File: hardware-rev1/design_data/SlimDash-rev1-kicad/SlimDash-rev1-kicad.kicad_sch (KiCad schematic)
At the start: 70 parts

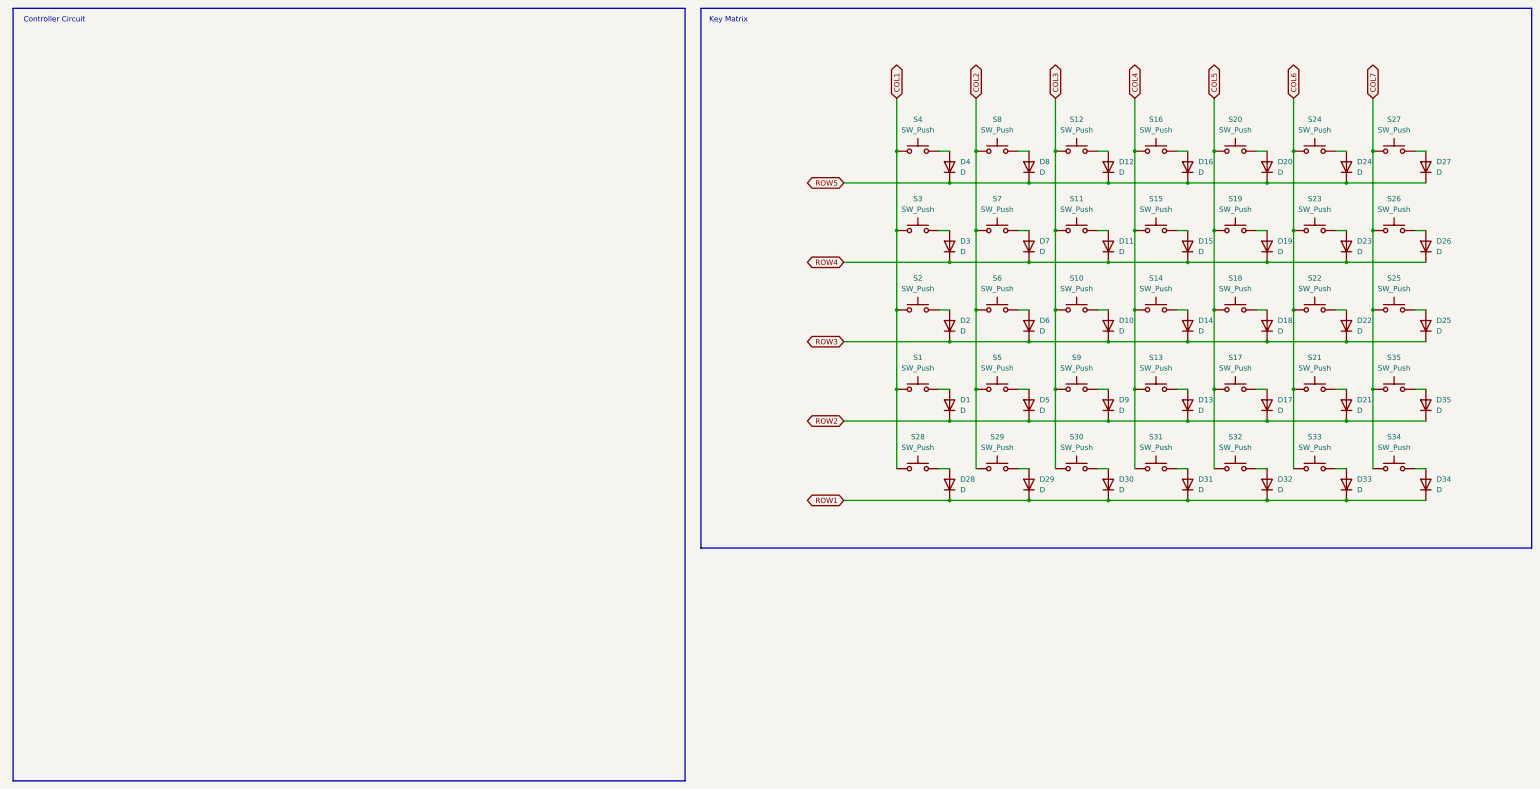
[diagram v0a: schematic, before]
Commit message: fix some positioning and net labels
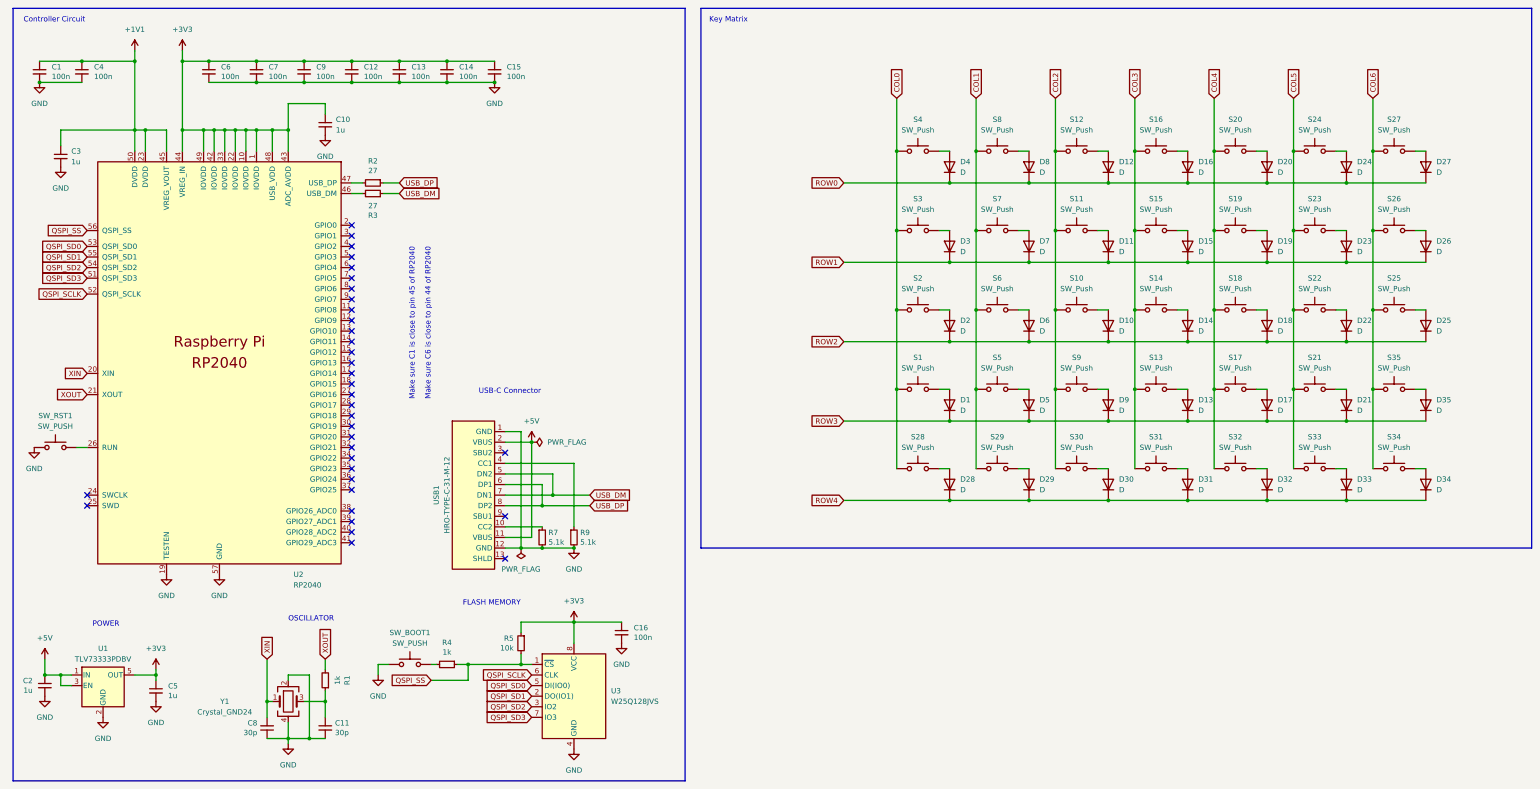
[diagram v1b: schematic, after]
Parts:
- added C1, C12, C13, C14, C15, C16, C4, C6, C7, C9: 100n, Capacitor_SMD:C_0402_1005Metric, symbol Device:C_Small
- added C10, C2, C3, C5: 1u, Capacitor_SMD:C_0402_1005Metric, symbol Device:C_Small
- added C11, C8: 30p, Capacitor_SMD:C_0402_1005Metric, symbol Device:C_Small
- added R1, R4: 1k, Resistor_SMD:R_0402_1005Metric, symbol Device:R_Small
- added R2, R3: 27, Resistor_SMD:R_0402_1005Metric, symbol Device:R_Small
- added R5: 10k, Resistor_SMD:R_0402_1005Metric, symbol Device:R_Small
- added R7, R9: 5.1k, Resistor_SMD:R_0402_1005Metric, symbol Device:R_Small
- added SW_BOOT1, SW_RST1: SW_PUSH, mzm_misc:SW_Tactile_Yushakobo 3x6x4.3mm, symbol Switch:SW_Push
- added U1: TLV73333PDBV, Package_TO_SOT_SMD:SOT-23-5, symbol Regulator_Linear:TLV73333PDBV
- added U2: RP2040, RP2040:RP2040-QFN-56, symbol ergoSHIFT-rev2:RP2040
- added U3: W25Q128JVS, Package_SO:SOIC-8_5.23x5.23mm_P1.27mm, symbol Memory_Flash:W25Q128JVS
- added USB1: HRO-TYPE-C-31-M-12, ai03-2725_Type-C:HRO-TYPE-C-31-M-12-Assembly, symbol ergoSHIFT-rev2:HRO-TYPE-C-31-M-12
- added Y1: Crystal_GND24, Crystal:Crystal_SMD_3225-4Pin_3.2x2.5mm, symbol Device:Crystal_GND24
- D1, D10, D11, D12, D13, D14, D15, D16, D17, D18, D19, D2, D20, D21, D22, D23, D24, D25, D26, D27, D28, D29, D3, D30, D31, D32, D33, D34, D35, D4, D5, D6, D7, D8, D9: footprint (none) -> Diode_SMD:D_SOD-123F; LCSC (none) -> C33962554
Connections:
- net COL7 is gone; now on net COL6: S25.1, S26.1, S27.1, S34.1, S35.1
- net COL1: now also S29.1, S5.1, S6.1, S7.1, S8.1; no longer S1.1, S2.1, S28.1, S3.1, S4.1
- net COL2: now also S10.1, S11.1, S12.1, S30.1, S9.1; no longer S29.1, S5.1, S6.1, S7.1, S8.1
- net COL3: now also S13.1, S14.1, S15.1, S16.1, S31.1; no longer S10.1, S11.1, S12.1, S30.1, S9.1
- net COL4: now also S17.1, S18.1, S19.1, S20.1, S32.1; no longer S13.1, S14.1, S15.1, S16.1, S31.1
- net COL5: now also S21.1, S22.1, S23.1, S24.1, S33.1; no longer S17.1, S18.1, S19.1, S20.1, S32.1
- net COL6: no longer S21.1, S22.1, S23.1, S24.1, S33.1
- net ROW1: now also D11.1 (K), D15.1 (K), D19.1 (K), D23.1 (K), D26.1 (K), D3.1 (K), D7.1 (K); no longer D28.1 (K), D29.1 (K), D30.1 (K), D31.1 (K), D32.1 (K), D33.1 (K), D34.1 (K)
- net ROW2: now also D10.1 (K), D14.1 (K), D18.1 (K), D2.1 (K), D22.1 (K), D25.1 (K), D6.1 (K); no longer D1.1 (K), D13.1 (K), D17.1 (K), D21.1 (K), D35.1 (K), D5.1 (K), D9.1 (K)
- net ROW3: now also D1.1 (K), D13.1 (K), D17.1 (K), D21.1 (K), D35.1 (K), D5.1 (K), D9.1 (K); no longer D10.1 (K), D14.1 (K), D18.1 (K), D2.1 (K), D22.1 (K), D25.1 (K), D6.1 (K)
- net ROW4: now also D28.1 (K), D29.1 (K), D30.1 (K), D31.1 (K), D32.1 (K), D33.1 (K), D34.1 (K); no longer D11.1 (K), D15.1 (K), D19.1 (K), D23.1 (K), D26.1 (K), D3.1 (K), D7.1 (K)
- net ROW5 renamed ROW0
- new net: C11.1, R1.1, Y1.3
- new net: R4.2, SW_BOOT1.2
- new net: R7.1, USB1.10 (CC2)
- new net: R9.1, USB1.4 (CC1)
- new net: SW_RST1.2, U2.26 (RUN)
- new net: R3.2, U2.46 (USB_DM)
- new net: R2.2, U2.47 (USB_DP)
- new net +1V1: C1.1, C3.1, C4.1, U2.23 (DVDD), U2.45 (VREG_VOUT), U2.50 (DVDD)
- new net +3V3: C10.1, C12.1, C13.1, C14.1, C15.1, C16.1, C5.1, C6.1, C7.1, C9.1, R5.1, U1.5 (OUT), U2.1 (IOVDD), U2.10 (IOVDD), U2.22 (IOVDD), U2.33 (IOVDD), U2.42 (IOVDD), U2.43 (ADC_AVDD), U2.44 (VREG_IN), U2.48 (USB_VDD), U2.49 (IOVDD), U3.8 (VCC)
- new net +5V: C2.1, U1.1 (IN), U1.3 (EN), USB1.11 (VBUS), USB1.2 (VBUS)
- new net COL0: S1.1, S2.1, S28.1, S3.1, S4.1
- new net GND: C1.2, C10.2, C11.2, C12.2, C13.2, C14.2, C15.2, C16.2, C2.2, C3.2, C4.2, C5.2, C6.2, C7.2, C8.1, C9.2, R7.2, R9.2, SW_BOOT1.1, SW_RST1.1, U1.2 (GND), U2.19 (TESTEN), U2.57 (GND), U3.4 (GND), USB1.1 (GND), USB1.12 (GND), Y1.2, Y1.4
- new net QSPI_SCLK: U2.52 (QSPI_SCLK), U3.6 (CLK)
- new net QSPI_SD0: U2.53 (QSPI_SD0), U3.5 (DI(IO0))
- new net QSPI_SD1: U2.55 (QSPI_SD1), U3.2 (DO(IO1))
- new net QSPI_SD2: U2.54 (QSPI_SD2), U3.3 (IO2)
- new net QSPI_SD3: U2.51 (QSPI_SD3), U3.7 (IO3)
- new net QSPI_SS: R4.1, R5.2, U2.56 (QSPI_SS), U3.1 (~{CS})
- new net USB_DM: R3.1, USB1.5 (DN2), USB1.7 (DN1)
- new net USB_DP: R2.1, USB1.6 (DP1), USB1.8 (DP2)
- new net XIN: C8.2, U2.20 (XIN), Y1.1
- new net XOUT: R1.2, U2.21 (XOUT)
- no-connect marks 0 -> 35
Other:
- note added: "FLASH MEMORY"
- note added: "Make sure C1 is close to pin 45 of RP2040"
- note added: "Make sure C6 is close to pin 44 of RP2040"
- note added: "OSCILLATOR"
- note added: "POWER"
- note added: "USB-C Connector"

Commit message: add more components to design data
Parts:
- added J1, J2: AudioJack4, Keebio-Parts:TRRS-PJ-320A, symbol Connector_Audio:AudioJack4
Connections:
- net +3V3: now also J1.1, J2.1
- net GND: now also J1.4, J2.4
- new net PIO_RX: J1.2, J2.3
- new net PIO_TX: J1.3, J2.2

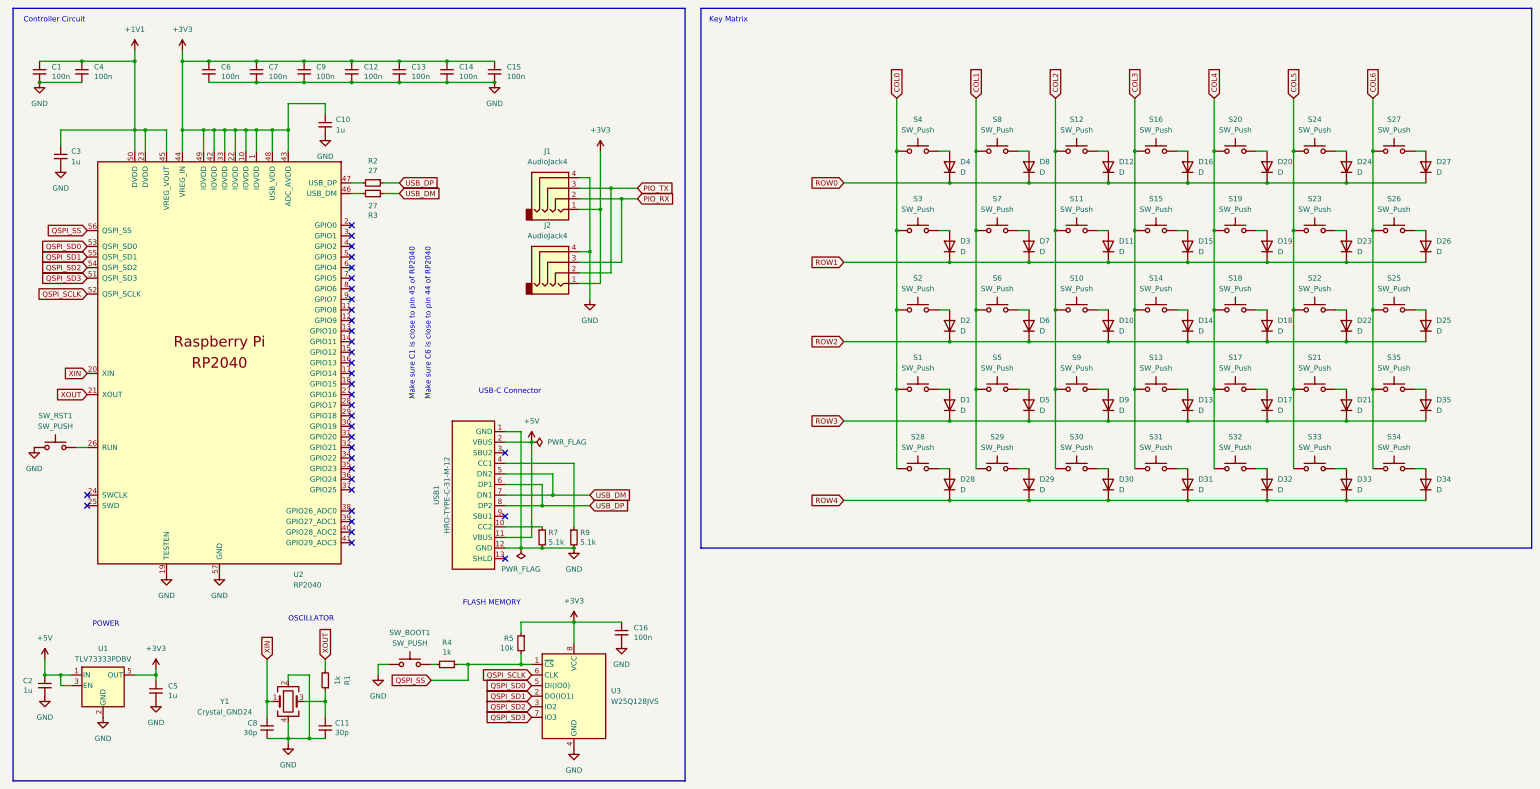
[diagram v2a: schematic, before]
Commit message: add surge protection
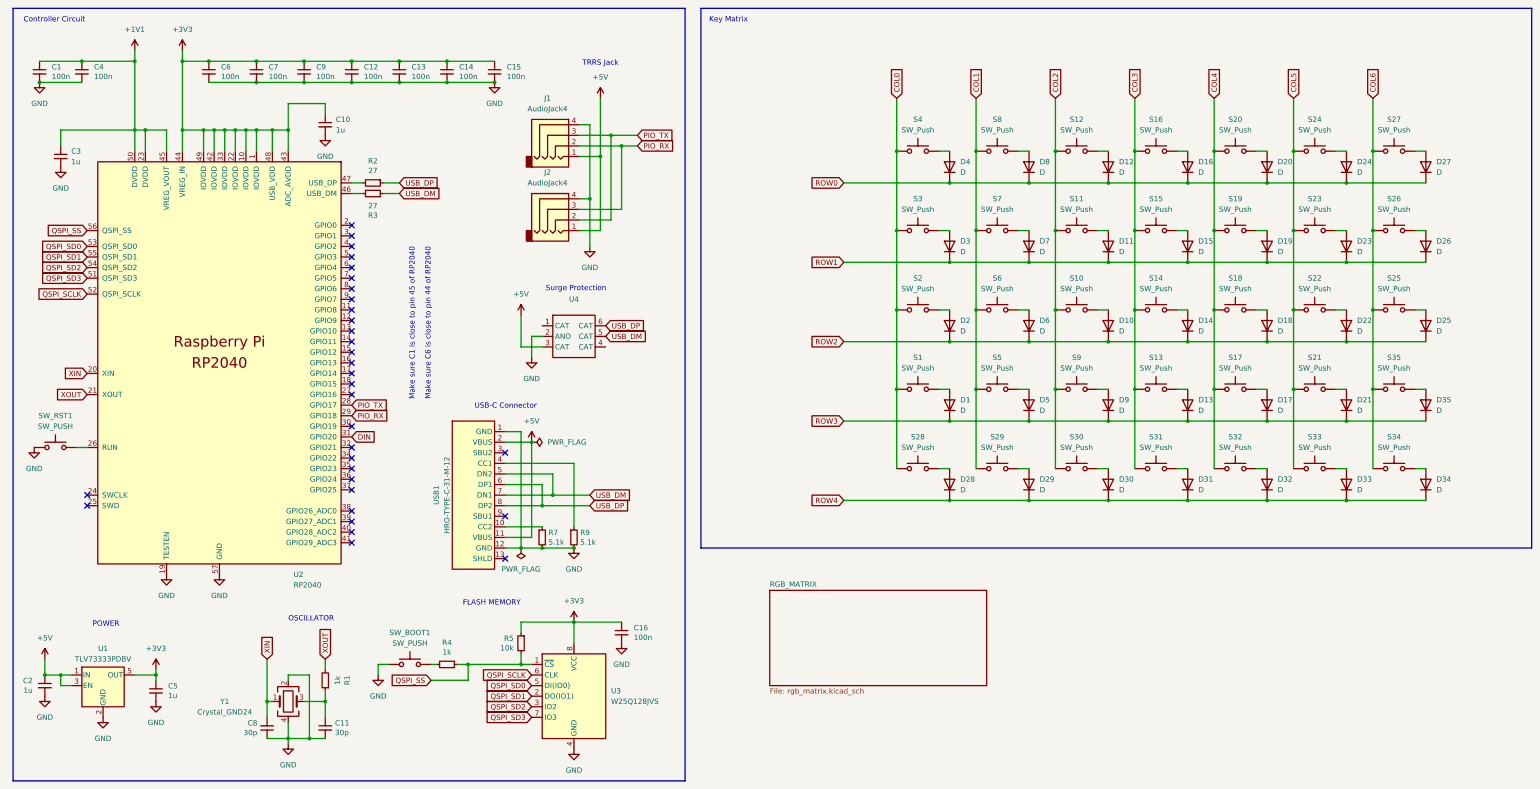
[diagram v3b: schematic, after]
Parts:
- added U4: ~, Keebio-Parts:SOT-363_SC-70-6, symbol mzm_kicad:onsemi_SMF05CT1G
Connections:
- net +3V3: no longer J1.1, J2.1
- net +5V: now also J1.1, J2.1, U4.3 (CAT)
- net GND: now also U4.2 (ANO)
- net PIO_RX: now also U2.29 (GPIO18)
- net PIO_TX: now also U2.28 (GPIO17)
- net USB_DM: now also U4.5 (CAT)
- net USB_DP: now also U4.6 (CAT)
- net DIN: now reaches U2.31 (GPIO20)
- no-connect marks 35 -> 32
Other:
- added sheet RGB_MATRIX (rgb_matrix.kicad_sch)
- note added: "Surge Protection"
- note added: "TRRS Jack"
- moved on the sheet: J1, J2

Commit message: more routing and fixing footprints
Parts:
- J1, J2: footprint Keebio-Parts:TRRS-PJ-320A -> mzm_misc:TRRS_jack
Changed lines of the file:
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@@
 			)
 		)
-		(property "Footprint" "Keebio-Parts:TRRS-PJ-320A"
+		(property "Footprint" "mzm_misc:TRRS_jack"
 			(at 147.32 46.99 0)
 			(effects
@@
 			)
 		)
-		(property "Footprint" "Keebio-Parts:TRRS-PJ-320A"
+		(property "Footprint" "mzm_misc:TRRS_jack"
 			(at 147.32 64.77 0)
 			(effects

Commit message: update submodule
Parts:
- USB1: footprint ai03-2725_Type-C:HRO-TYPE-C-31-M-12-Assembly -> mzm_LCSC:USB-C_SMD-TYPE-C-31-M-12
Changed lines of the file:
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@@
 			)
 		)
-		(property "Footprint" "ai03-2725_Type-C:HRO-TYPE-C-31-M-12-Assembly"
+		(property "Footprint" "mzm_LCSC:USB-C_SMD-TYPE-C-31-M-12"
 			(at 120.65 133.35 90)
 			(effects

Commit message: finalize pcb layout
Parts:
- added C17, C18: 10u, Capacitor_SMD:C_0402_1005Metric, symbol Device:C
- D1, D10, D11, D12, D13, D14, D15, D16, D17, D18, D19, D2, D20, D21, D22, D23, D24, D25, D26, D27, D28, D29, D3, D30, D31, D32, D33, D34, D35, D4, D5, D6, D7, D8, D9: LCSC C33962554 -> C2908120
- U4: value ~ -> SMF05CT1G; LCSC (none) -> C15879
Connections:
- net +5V: now also C17.1, C18.1
- net COL0: now also U2.2 (GPIO0)
- net COL1: now also U2.3 (GPIO1)
- net COL2: now also U2.5 (GPIO3)
- net COL3: now also U2.7 (GPIO5)
- net COL4: now also U2.11 (GPIO8)
- net COL5: now also U2.9 (GPIO7)
- net COL6: now also U2.12 (GPIO9)
- net GND: now also C17.2, C18.2
- net ROW0: now also U2.4 (GPIO2)
- net ROW1: now also U2.6 (GPIO4)
- net ROW2: now also U2.8 (GPIO6)
- net ROW3: now also U2.14 (GPIO11)
- net ROW4: now also U2.13 (GPIO10)
- no-connect marks 32 -> 20
